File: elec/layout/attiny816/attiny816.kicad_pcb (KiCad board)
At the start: 2 copper layers, 3 parts, among them U1 ?

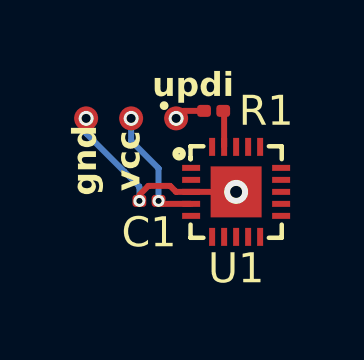
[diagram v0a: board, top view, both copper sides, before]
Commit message: added 3v reg + layout edits
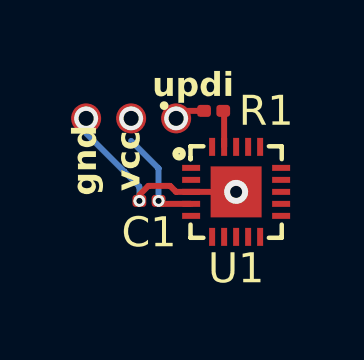
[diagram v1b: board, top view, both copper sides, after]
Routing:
- net vcc: track 4.26 -> 3.51 mm
- net gnd: track 6.97 -> 6.47 mm
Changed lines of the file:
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@@
 	(gr_circle
 		(center 142.75 119.75)
-		(end 143.05 119.75)
+		(end 143.15 119.75)
 		(stroke
 			(width 0.2)
@@
 	(gr_circle
 		(center 141.25 119.75)
-		(end 141.55 119.75)
+		(end 141.65 119.75)
 		(stroke
 			(width 0.2)
@@
 	(gr_circle
 		(center 144.25 119.75)
-		(end 144.55 119.75)
+		(end 144.65 119.75)
 		(stroke
 			(width 0.2)
@@
 	(via
 		(at 142.75 119.75)
-		(size 0.5)
-		(drill 0.3)
+		(size 0.8)
+		(drill 0.5)
 		(layers "F.Cu" "B.Cu")
 		(free yes)
@@
 	)
 	(segment
-		(start 142.75 120.5)
-		(end 142.75 119.75)
-		(width 0.2)
-		(layer "B.Cu")
-		(net 1)
-	)
-	(segment
 		(start 143.665 122.5)
 		(end 143.665 121.415)
@@
 	(via
 		(at 141.25 119.75)
-		(size 0.5)
-		(drill 0.3)
+		(size 0.8)
+		(drill 0.5)
 		(layers "F.Cu" "B.Cu")
 		(free yes)
@@
 	)
 	(segment
-		(start 141.25 119.75)
-		(end 141.25 120.25)
-		(width 0.2)
-		(layer "B.Cu")
-		(net 2)
-	)
-	(segment
 		(start 146.2 122.2)
 		(end 146.25 122.2)
@@
 	(via
 		(at 144.25 119.75)
-		(size 0.5)
-		(drill 0.3)
-		(layers "F.Cu" "B.Cu")
-		(free yes)
+		(size 0.8)
+		(drill 0.5)
+		(layers "F.Cu" "B.Cu")
+		(free yes)

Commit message: fixed maybe
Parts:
- moved R1 27.8 mm to (173.2, 117.7), turned to -90 degrees
- moved C1 27.3 mm to (170.6, 120.9)
- moved U1 27.3 mm to (173.5, 120.6)
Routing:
- net pb1: track 0.00 -> 27.9 mm, vias 0 -> 2
- net 22: track 0.00 -> 6.39 mm, vias 0 -> 4
- net gnd: track 6.47 -> 3.48 mm, vias 3 -> 1
- net vcc: track 3.51 -> 1.13 mm, vias 2 -> 0
- net updi: track 1.17 -> 2.75 mm
- net pa3_extclk: track 0.00 -> 1.05 mm
- net pa7: track 0.00 -> 1.02 mm, vias 0 -> 1
- net 23: vias 0 -> 4
